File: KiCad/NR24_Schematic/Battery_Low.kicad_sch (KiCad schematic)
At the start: 5 parts

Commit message: update
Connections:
- net LV_pwr renamed LV_High
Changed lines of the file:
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@@
     (effects (font (size 1.27 1.27) bold) (justify left))
   )
-  (hierarchical_label "LV_pwr" (shape input) (at 78.74 77.47 90) (fields_autoplaced)
+  (hierarchical_label "LV_High" (shape input) (at 78.74 77.47 90) (fields_autoplaced)
     (effects (font (size 1.27 1.27) (thickness 0.254) bold (color 255 0 0 1)) (justify left))
   )

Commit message: Now it is pretty :)
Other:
- moved on the sheet: D7, RL1

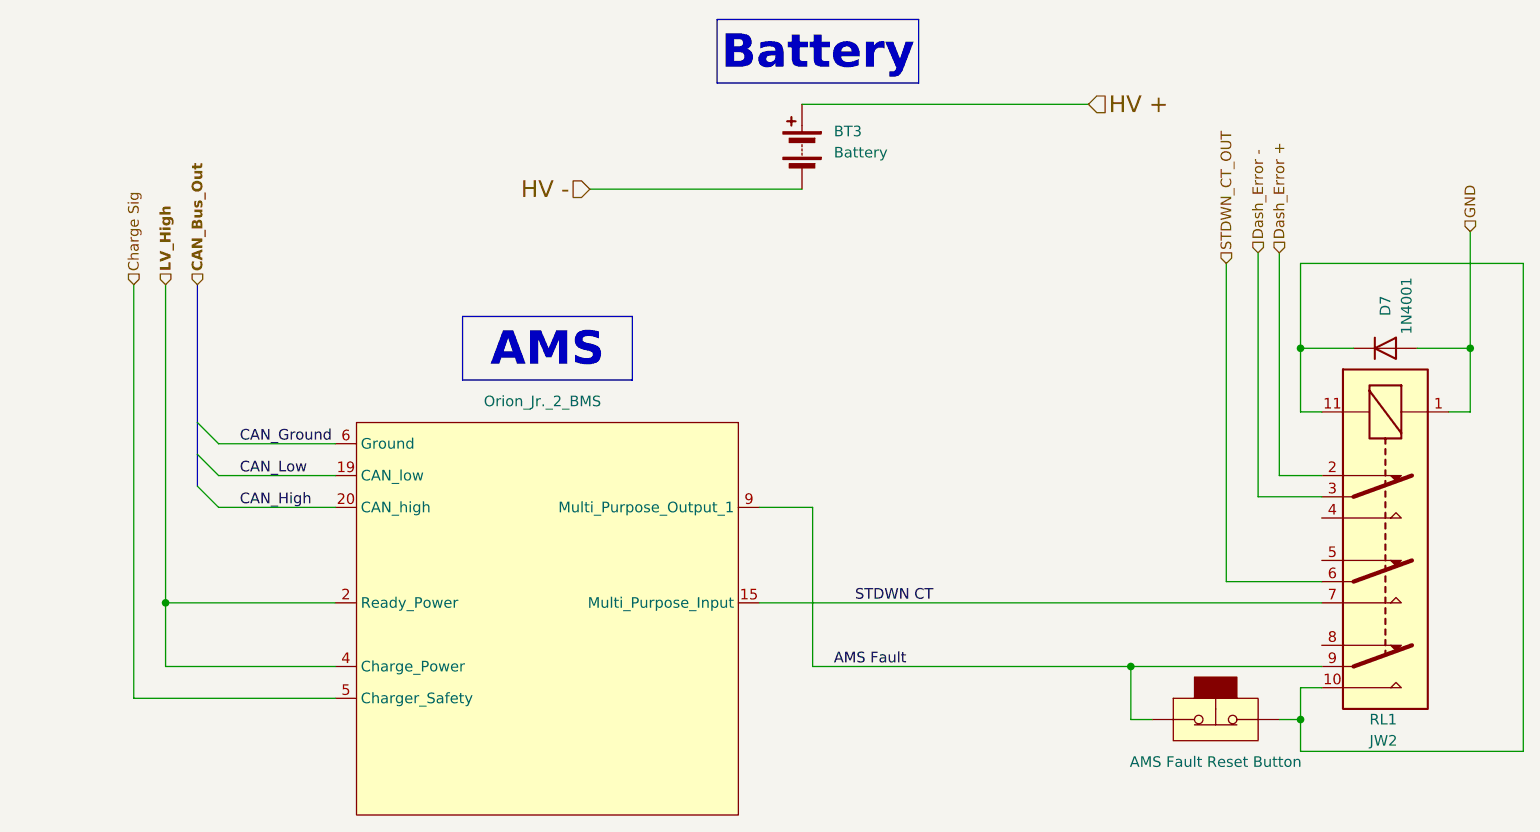
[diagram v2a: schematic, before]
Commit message: added accumulator info
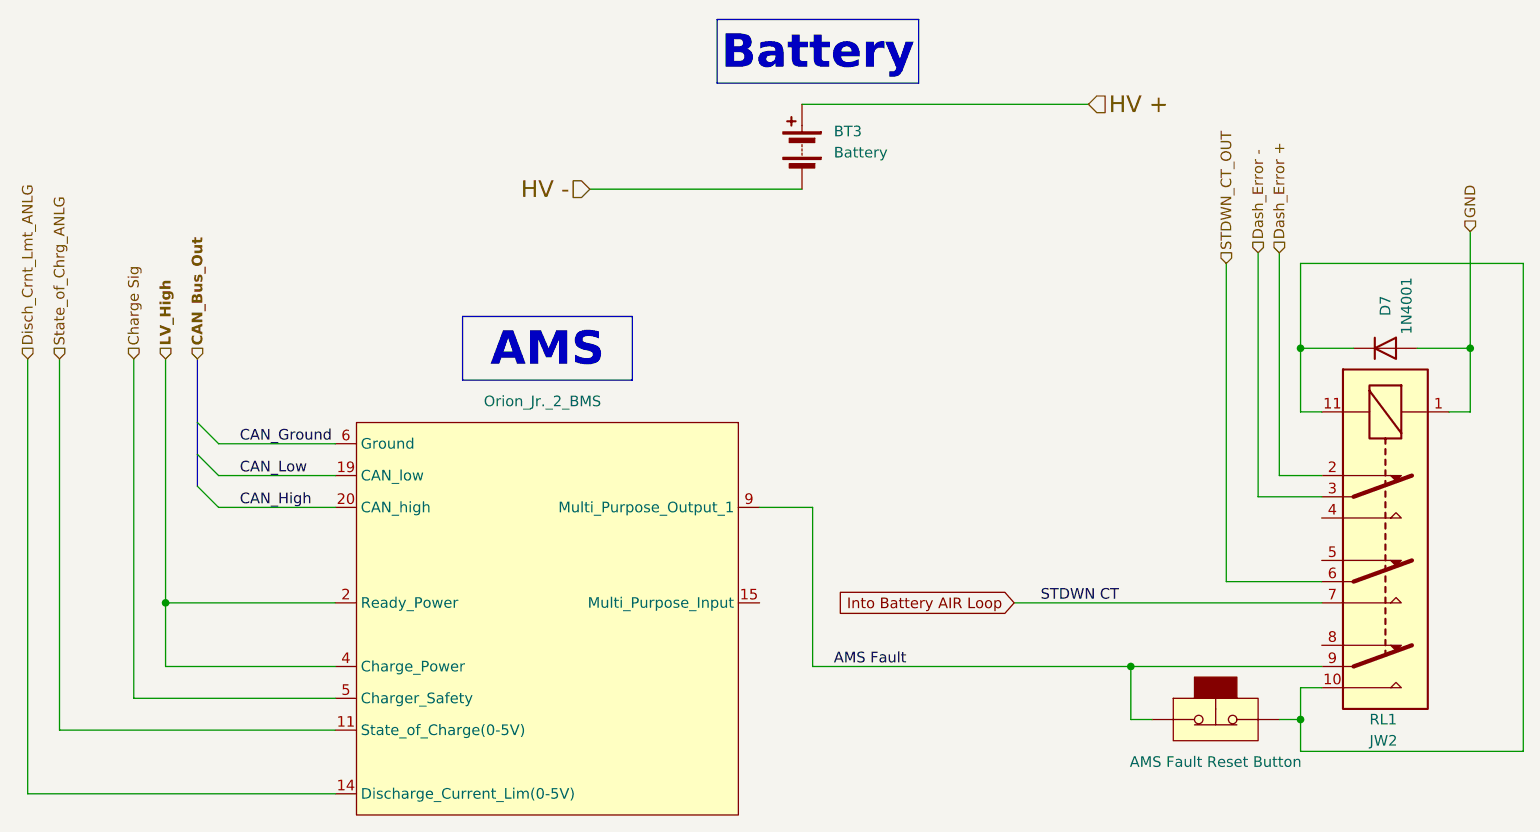
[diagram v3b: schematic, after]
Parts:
- removed U?: Orion_Jr._2_BMS, symbol CamachosSymbols:Sevcon_Gen4_Size6
- added U?: Orion_Jr._2_BMS, symbol CamachosSymbols:Sevcon_Gen4_Size6
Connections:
- net AMS Fault: now also U?.9 (Multi_Purpose_Output_1)
- net CAN_Ground: now also U?.6 (Ground)
- net CAN_High: now also U?.20 (CAN_high)
- net CAN_Low: now also U?.19 (CAN_low)
- net Charge Sig: now also U?.5 (Charger_Safety)
- net LV_High: now also U?.2 (Ready_Power), U?.4 (Charge_Power)
- net STDWN CT renamed Into Battery AIR Loop
- new net Disch_Crnt_Lmt_ANLG: U?.14 (Discharge_Current_Lim(0-5V))
- new net State_of_Chrg_ANLG: U?.11 (State_of_Charge(0-5V))

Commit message: first iteration
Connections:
- net Disch_Crnt_Lmt_ANLG: no longer names the net of U?.14 (Discharge_Current_Lim(0-5V))
- net State_of_Chrg_ANLG: no longer names the net of U?.11 (State_of_Charge(0-5V))
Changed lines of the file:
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@@
-    (stroke (width 0) (type default))
-  )
-  (wire (pts (xy 62.23 82.55) (xy 62.23 134.62))
     (stroke (width 0) (type default))
   )
@@
     (stroke (width 0) (type default))
   )
-  (wire (pts (xy 66.04 82.55) (xy 66.04 127))
-    (stroke (width 0) (type default))
-  )
   (wire (pts (xy 214.63 125.73) (xy 214.63 129.54))
     (stroke (width 0) (type default))
@@
     (stroke (width 0) (type default))
   )
-  (wire (pts (xy 99.06 127) (xy 66.04 127))
-    (stroke (width 0) (type default))
-  )
   (wire (pts (xy 214.63 129.54) (xy 241.3 129.54))
     (stroke (width 0) (type default))
@@
   )
   (wire (pts (xy 194.31 125.73) (xy 196.85 125.73))
-    (stroke (width 0) (type default))
-  )
-  (wire (pts (xy 99.06 134.62) (xy 62.23 134.62))
     (stroke (width 0) (type default))
   )
@@
     (effects (font (size 1.27 1.27) bold) (justify left))
   )
-  (hierarchical_label "Disch_Crnt_Lmt_ANLG" (shape input) (at 62.23 82.55 90) (fields_autoplaced)
-    (effects (font (size 1.27 1.27)) (justify left))
-  )
   (hierarchical_label "GND" (shape input) (at 234.95 67.31 90) (fields_autoplaced)
     (effects (font (size 1.27 1.27)) (justify left))
@@
     (effects (font (size 1.27 1.27)) (justify left))
   )
-  (hierarchical_label "State_of_Chrg_ANLG" (shape input) (at 66.04 82.55 90) (fields_autoplaced)
-    (effects (font (size 1.27 1.27)) (justify left))
-  )

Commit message: Pre Break Schematic
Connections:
- net AMS Fault: no longer names the net of RL1.9, SW?.1 (A), U?.9 (Multi_Purpose_Output_1)
- net CAN_Ground: no longer names the net of U?.6 (Ground)
- net CAN_High: no longer names the net of U?.20 (CAN_high)
- net CAN_Low: no longer names the net of U?.19 (CAN_low)
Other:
- note added: "AMS Fault"
- note added: "CAN_Ground"
- note added: "CAN_High"
- note added: "CAN_Low"
- note added: "SHTDWN CRCT"
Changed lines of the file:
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@@
     (effects (font (size 4 4) (thickness 0.8) bold (color 0 0 0 1)))
   )
-  (label "AMS Fault" (at 158.75 119.38 0) (fields_autoplaced)
-    (effects (font (size 1.27 1.27)) (justify left bottom))
-  )
-  (label "CAN_Ground" (at 87.63 92.71 0) (fields_autoplaced)
-    (effects (font (size 1.27 1.27)) (justify left bottom))
-  )
-  (label "CAN_Low" (at 87.63 96.52 0) (fields_autoplaced)
-    (effects (font (size 1.27 1.27)) (justify left bottom))
-  )
-  (label "STDWN CT" (at 183.515 111.76 0) (fields_autoplaced)
-    (effects (font (size 1.27 1.27)) (justify left bottom))
-  )
-  (label "CAN_High" (at 87.63 100.33 0) (fields_autoplaced)
+  (text "CAN_Low" (at 86.36 96.52 0)
+    (effects (font (size 1.27 1.27)) (justify left bottom))
+  )
+  (text "CAN_Ground" (at 86.36 92.71 0)
+    (effects (font (size 1.27 1.27)) (justify left bottom))
+  )
+  (text "AMS Fault" (at 170.815 119.38 0)
+    (effects (font (size 1.27 1.27)) (justify left bottom))
+  )
+  (text "SHTDWN CRCT" (at 184.15 111.76 0)
+    (effects (font (size 1.27 1.27)) (justify left bottom))
+  )
+  (text "CAN_High" (at 86.36 100.33 0)
     (effects (font (size 1.27 1.27)) (justify left bottom))
   )
@@
     (pin "2")
     (instances
-      (project "Car_TractiveSystem_MAIN"
+      (project "NR24_Schematic"
         (path "/588b5c14-1813-4e1d-9dbe-940839ecebe3/600c7e11-1cec-4d55-8384-7f41b96b4c2b"
           (reference "BT3") (unit 1)
         )
         (path "/588b5c14-1813-4e1d-9dbe-940839ecebe3/0f310f4a-0260-43da-aff0-c6bb29799d15"
-          (reference "BT1") (unit 1)
+          (reference "BT2") (unit 1)
         )
       )
@@
     (pin "9")
     (instances
-      (project "Car_TractiveSystem_MAIN"
+      (project "NR24_Schematic"
         (path "/588b5c14-1813-4e1d-9dbe-940839ecebe3"
           (reference "U?") (unit 1)
         )
         (path "/588b5c14-1813-4e1d-9dbe-940839ecebe3/0f310f4a-0260-43da-aff0-c6bb29799d15"
-          (reference "U5") (unit 1)
+          (reference "U8") (unit 1)
         )
         (path "/588b5c14-1813-4e1d-9dbe-940839ecebe3/600c7e11-1cec-4d55-8384-7f41b96b4c2b"
@@
     (pin "9")
     (instances
-      (project "Car_TractiveSystem_MAIN"
+      (project "NR24_Schematic"
         (path "/588b5c14-1813-4e1d-9dbe-940839ecebe3/600c7e11-1cec-4d55-8384-7f41b96b4c2b"
           (reference "RL1") (unit 1)
         )
         (path "/588b5c14-1813-4e1d-9dbe-940839ecebe3/0f310f4a-0260-43da-aff0-c6bb29799d15"
-          (reference "RL4") (unit 1)
+          (reference "RL3") (unit 1)
         )
       )
@@
     (pin "2")
     (instances
-      (project "Car_TractiveSystem_MAIN"
+      (project "NR24_Schematic"
         (path "/588b5c14-1813-4e1d-9dbe-940839ecebe3/600c7e11-1cec-4d55-8384-7f41b96b4c2b"
           (reference "D7") (unit 1)
@@
     (pin "2")
     (instances
-      (project "Car_TractiveSystem_MAIN"
+      (project "NR24_Schematic"
         (path "/588b5c14-1813-4e1d-9dbe-940839ecebe3"
           (reference "SW?") (unit 1)
@@
         )
         (path "/588b5c14-1813-4e1d-9dbe-940839ecebe3/0f310f4a-0260-43da-aff0-c6bb29799d15"
-          (reference "SW12") (unit 1)
-        )
-      )
+          (reference "SW11") (unit 1)
+        )
+      )
